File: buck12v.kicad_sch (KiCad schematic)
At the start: 20 parts, among them J5 Conn_01x02, J6 Conn_01x02, Q10 Q_NMOS, Q7 Q_NMOS, Q8 Q_NMOS, U2 LM5148RGYR

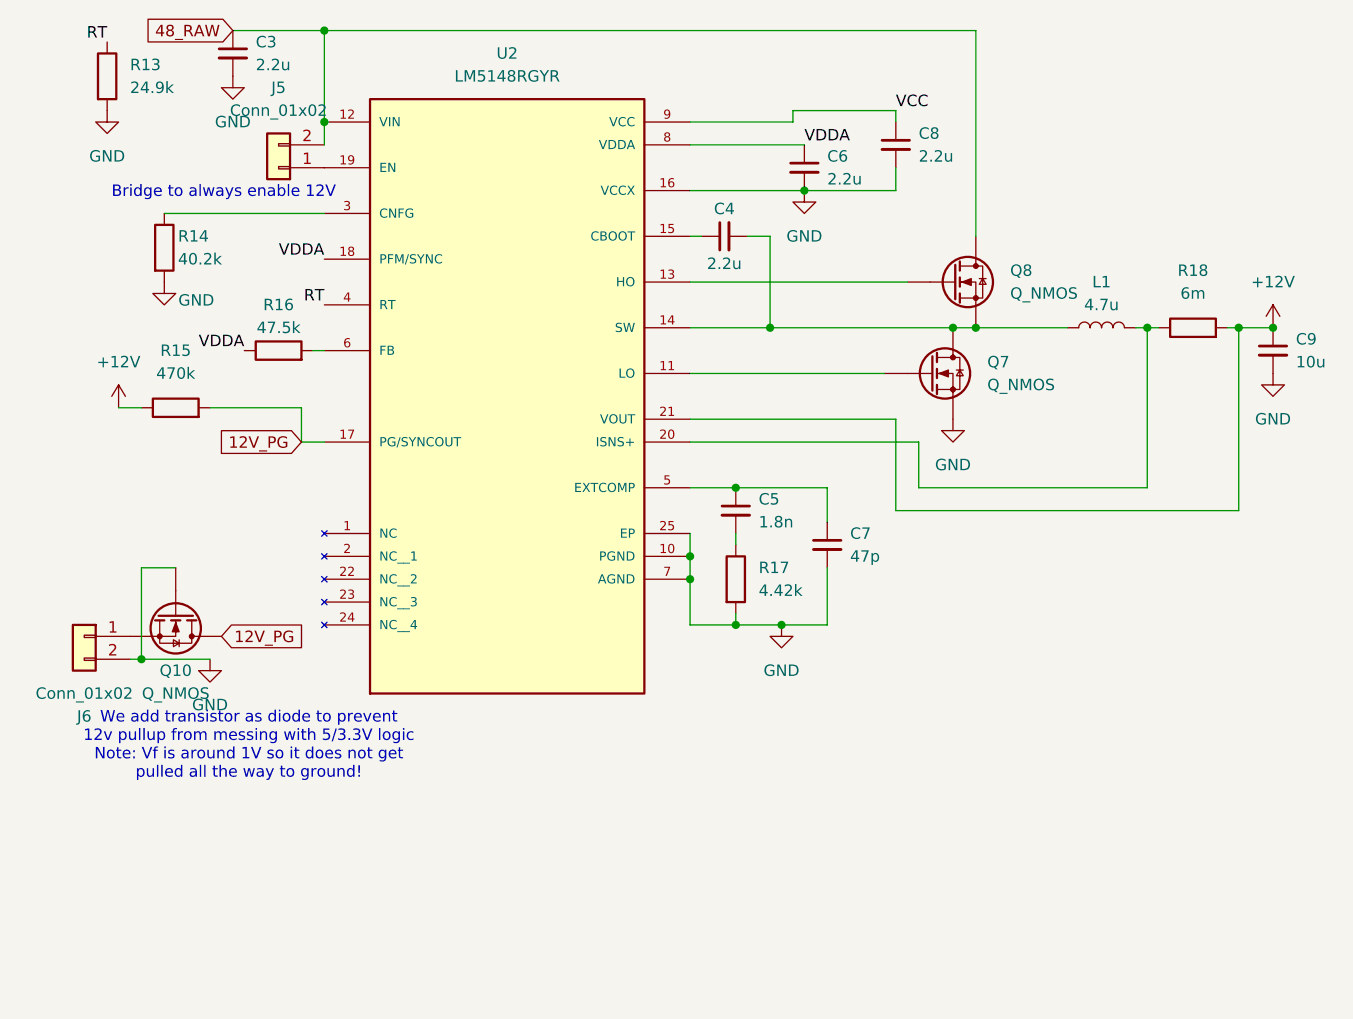
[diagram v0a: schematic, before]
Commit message: added footprints and standardized EN headers
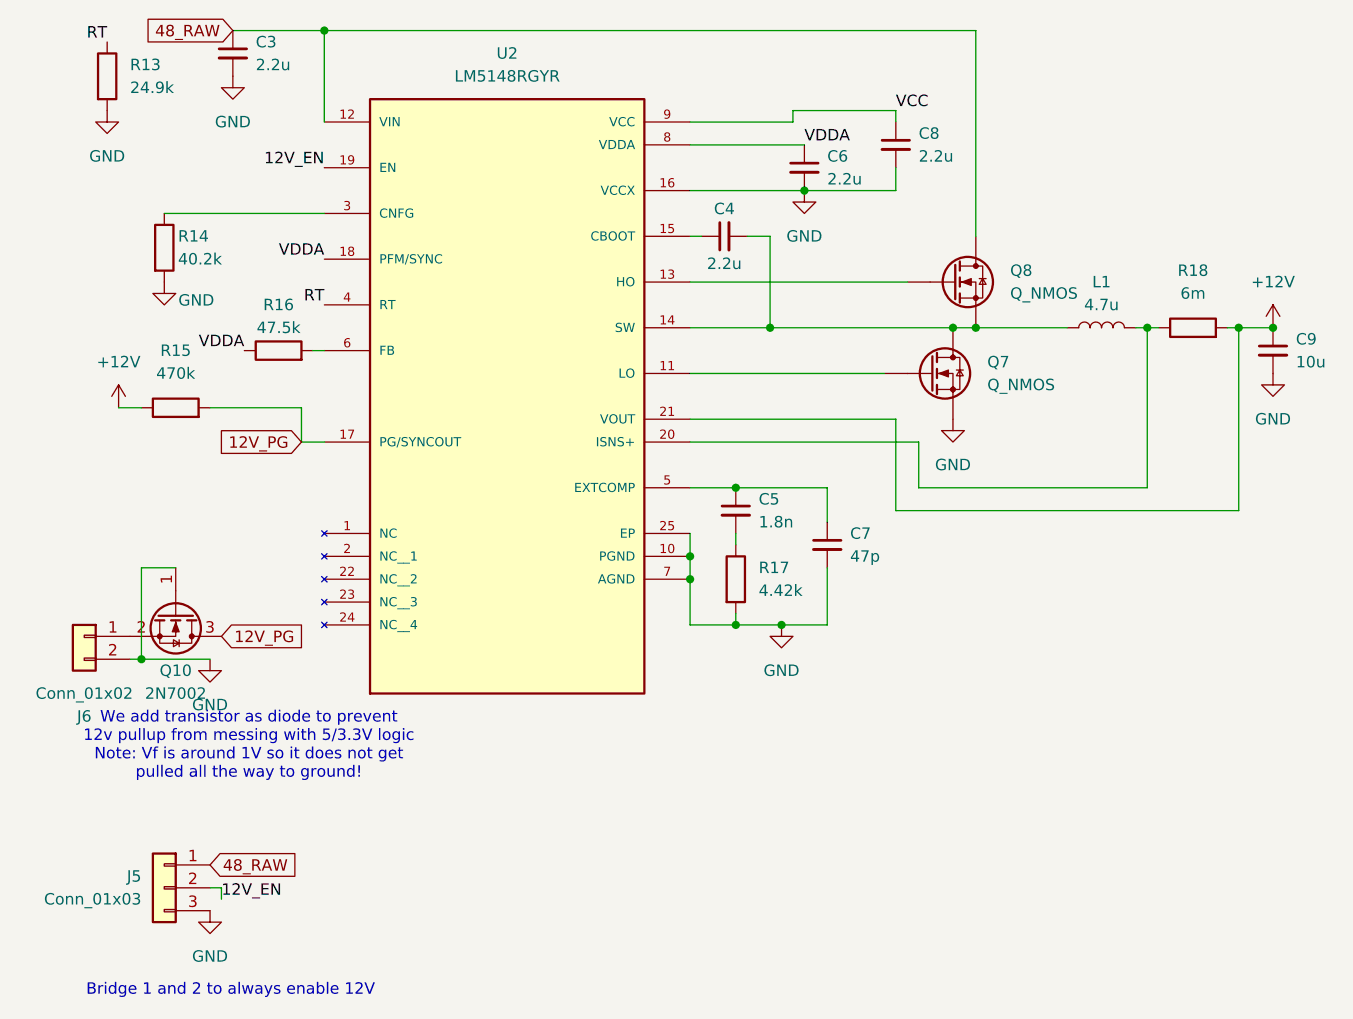
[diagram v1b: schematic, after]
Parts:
- removed J5: Conn_01x02, symbol Connector_Generic:Conn_01x02
- removed Q10: Q_NMOS, symbol Device:Q_NMOS
- added J5: Conn_01x03, Connector_PinHeader_2.54mm:PinHeader_1x03_P2.54mm_Vertical, symbol Connector_Generic:Conn_01x03
- added Q10: 2N7002, Package_TO_SOT_SMD:SOT-23, symbol Transistor_FET:2N7002
- J6: footprint (none) -> Connector_PinHeader_2.54mm:PinHeader_1x02_P2.54mm_Vertical
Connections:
- net 12V_PG: now also Q10.3 (D)
- net 48_RAW: now also J5.1 (Pin_1)
- net GND: now also J5.3 (Pin_3), Q10.1 (G)
- net at J6.1 (Pin_1): now also Q10.2 (S)
- net 12V_EN: now reaches U2.19 (EN)
- net 12V_EN: now also J5.2 (Pin_2)
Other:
- note added: "Bridge 1 and 2 to always enable 12V"
- note removed: "Bridge to always enable 12V"

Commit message: pcb routing
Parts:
- R15: footprint (none) -> Resistor_SMD:R_0201_0603Metric_Pad0.64x0.40mm_HandSolder
- R18: value 6m -> 6m 1W; footprint (none) -> Resistor_SMD:R_1206_3216Metric_Pad1.30x1.75mm_HandSolder
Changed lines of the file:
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@@
 			)
 		)
-		(property "Datasheet" "~"
+		(property "Datasheet" "CODACA"
 			(at 129.54 49.53 0)
 			(effects
@@
 			)
 		)
-		(property "Footprint" ""
+		(property "Footprint" "Resistor_SMD:R_0201_0603Metric_Pad0.64x0.40mm_HandSolder"
 			(at 26.67 60.198 90)
 			(effects
@@
 			)
 		)
-		(property "Value" "6m"
+		(property "Value" "6m 1W"
 			(at 139.7 45.72 90)
 			(effects
@@
 			)
 		)
-		(property "Footprint" ""
+		(property "Footprint" "Resistor_SMD:R_1206_3216Metric_Pad1.30x1.75mm_HandSolder"
 			(at 139.7 51.308 90)
 			(effects

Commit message: final push
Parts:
- L1: value 4.7u -> 3.7; footprint (none) -> footprints:P1173.372NL
- Q7, Q8: footprint (none) -> Package_TO_SOT_SMD:TO-252-2; symbol Device:Q_NMOS -> xt90:NMOS_for_footprint
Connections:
- net 48_RAW: now also Q8.2 (D); no longer Q8.D
- net GND: now also Q7.3 (S); no longer Q7.S
- net at C4.2, L1.1, U2.14 (SW): now also Q7.2 (D), Q8.3 (S); no longer Q7.D, Q8.S
- net at U2.11 (LO): now also Q7.1 (G); no longer Q7.G
- net at U2.13 (HO): now also Q8.1 (G); no longer Q8.G
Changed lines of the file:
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@@
 		)
 		(instances
+			(project "buck12v"
+				(path "/77db3944-8136-4a9d-8d46-d8c78d169ccf"
+					(reference "Q?")
+					(unit 1)
+				)
+			)
 			(project ""
 				(path "/883cb7fa-3eb5-48d4-9cde-7c11307d94f0/ccf07133-5d0c-4081-9a30-ebff06623cf2"
@@
 	)
 	(symbol
-		(lib_id "Device:Q_NMOS")
+		(lib_id "xt90:NMOS_for_footprint")
 		(at 110.49 54.61 0)
 		(unit 1)
@@
 			)
 		)
-		(property "Footprint" ""
+		(property "Footprint" "Package_TO_SOT_SMD:TO-252-2"
 			(at 115.57 52.07 0)
 			(effects
@@
 			)
 		)
-		(pin "S"
-		)
-		(pin "D"
-		)
-		(pin "G"
+		(pin "2"
+		)
+		(pin "3"
+		)
+		(pin "1"
 		)
 		(instances
@@
 		)
 		(instances
+			(project "buck12v"
+				(path "/77db3944-8136-4a9d-8d46-d8c78d169ccf"
+					(reference "J?")
+					(unit 1)
+				)
+			)
 			(project "doggie_board"
 				(path "/883cb7fa-3eb5-48d4-9cde-7c11307d94f0/ccf07133-5d0c-4081-9a30-ebff06623cf2"
@@
 			)
 		)
-		(property "Value" "4.7u"
+		(property "Value" "3.7"
 			(at 129.54 46.99 90)
 			(effects
@@
 			)
 		)
-		(property "Footprint" ""
+		(property "Footprint" "footprints:P1173.372NL"
 			(at 129.54 49.53 0)
 			(effects
@@
 		)
 		(instances
+			(project "buck12v"
+				(path "/77db3944-8136-4a9d-8d46-d8c78d169ccf"
+					(reference "J?")
+					(unit 1)
+				)
+			)
 			(project "doggie_board"
 				(path "/883cb7fa-3eb5-48d4-9cde-7c11307d94f0/ccf07133-5d0c-4081-9a30-ebff06623cf2"
@@
 		)
 		(instances
+			(project "buck12v"
+				(path "/77db3944-8136-4a9d-8d46-d8c78d169ccf"
+					(reference "R?")
+					(unit 1)
+				)
+			)
 			(project ""
 				(path "/883cb7fa-3eb5-48d4-9cde-7c11307d94f0/ccf07133-5d0c-4081-9a30-ebff06623cf2"
@@
 		)
 		(instances
+			(project "buck12v"
+				(path "/77db3944-8136-4a9d-8d46-d8c78d169ccf"
+					(reference "#PWR?")
+					(unit 1)
+				)
+			)
 			(project "doggie_board"
 				(path "/883cb7fa-3eb5-48d4-9cde-7c11307d94f0/ccf07133-5d0c-4081-9a30-ebff06623cf2"
@@
 	)
 	(symbol
-		(lib_id "Device:Q_NMOS")
+		(lib_id "xt90:NMOS_for_footprint")
 		(at 113.03 44.45 0)
 		(unit 1)
@@
 			)
 		)
-		(property "Footprint" ""
+		(property "Footprint" "Package_TO_SOT_SMD:TO-252-2"
 			(at 118.11 41.91 0)
 			(effects
@@
 			)
 		)
-		(pin "S"
-		)
-		(pin "D"
-		)
-		(pin "G"
+		(pin "1"
+		)
+		(pin "2"
+		)
+		(pin "3"
 		)
 		(instances
@@
 		)
 		(instances
+			(project "buck12v"
+				(path "/77db3944-8136-4a9d-8d46-d8c78d169ccf"
+					(reference "#PWR?")
+					(unit 1)
+				)
+			)
 			(project ""
 				(path "/883cb7fa-3eb5-48d4-9cde-7c11307d94f0/ccf07133-5d0c-4081-9a30-ebff06623cf2"
@@
 		)
 		(instances
+			(project "buck12v"
+				(path "/77db3944-8136-4a9d-8d46-d8c78d169ccf"
+					(reference "#PWR?")
+					(unit 1)
+				)
+			)
 			(project ""
 				(path "/883cb7fa-3eb5-48d4-9cde-7c11307d94f0/ccf07133-5d0c-4081-9a30-ebff06623cf2"

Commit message: om suggestions
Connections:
- net switch 12v: now reaches C4.2, L1.1, Q7.2 (D), Q8.3 (S), U2.14 (SW)
- net low_fet: now reaches Q7.1 (G), U2.11 (LO)
- net sense: now reaches L1.2, R18.1, U2.20 (ISNS+)
- net high_fet: now reaches Q8.1 (G), U2.13 (HO)
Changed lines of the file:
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@@
+		)
+	)
+	(label "high_fet"
+		(at 100.33 44.45 0)
+		(effects
+			(font
+				(size 1.27 1.27)
+			)
+			(justify left bottom)
 		)
 	)
@@
 			)
 			(justify right bottom)
+		)
+	)
+	(label "low_fet"
+		(at 95.25 54.61 0)
+		(effects
+			(font
+				(size 1.27 1.27)
+			)
+			(justify left bottom)
 		)
 	)
@@
 		)
 	)
+	(label "sense"
+		(at 134.62 49.53 90)
+		(effects
+			(font
+				(size 1.27 1.27)
+			)
+			(justify left bottom)
+		)
+	)
 	(label "RT"
 		(at 43.18 46.99 180)
@@
 		)
 	)
+	(label "switch 12v"
+		(at 95.25 49.53 0)
+		(effects
+			(font
+				(size 1.27 1.27)
+			)
+			(justify left bottom)
+		)
+	)

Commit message: fixed footprintns
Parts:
- C3, C4, C5, C6, C7, C8, C9: footprint Capacitor_SMD:C_0201_0603Metric_Pad0.64x0.40mm_HandSolder -> Capacitor_SMD:C_0603_1608Metric_Pad1.08x0.95mm_HandSolder
- R13, R14, R15, R16, R17: footprint Resistor_SMD:R_0201_0603Metric_Pad0.64x0.40mm_HandSolder -> Resistor_SMD:R_0603_1608Metric_Pad0.98x0.95mm_HandSolder
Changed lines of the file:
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@@
 			)
 		)
-		(property "Footprint" "Resistor_SMD:R_0201_0603Metric_Pad0.64x0.40mm_HandSolder"
+		(property "Footprint" "Resistor_SMD:R_0603_1608Metric_Pad0.98x0.95mm_HandSolder"
 			(at 23.622 40.64 90)
 			(effects
@@
 			)
 		)
-		(property "Footprint" "Capacitor_SMD:C_0201_0603Metric_Pad0.64x0.40mm_HandSolder"
+		(property "Footprint" "Capacitor_SMD:C_0603_1608Metric_Pad1.08x0.95mm_HandSolder"
 			(at 87.63 39.37 0)
 			(effects
@@
 			)
 		)
-		(property "Footprint" "Capacitor_SMD:C_0201_0603Metric_Pad0.64x0.40mm_HandSolder"
+		(property "Footprint" "Capacitor_SMD:C_0603_1608Metric_Pad1.08x0.95mm_HandSolder"
 			(at 148.59 52.07 0)
 			(effects
@@
 			)
 		)
-		(property "Footprint" "Capacitor_SMD:C_0201_0603Metric_Pad0.64x0.40mm_HandSolder"
+		(property "Footprint" "Capacitor_SMD:C_0603_1608Metric_Pad1.08x0.95mm_HandSolder"
 			(at 33.02 19.05 0)
 			(effects
@@
 			)
 		)
-		(property "Footprint" "Capacitor_SMD:C_0201_0603Metric_Pad0.64x0.40mm_HandSolder"
+		(property "Footprint" "Capacitor_SMD:C_0603_1608Metric_Pad1.08x0.95mm_HandSolder"
 			(at 88.9 69.85 0)
 			(effects
@@
 			)
 		)
-		(property "Footprint" "Resistor_SMD:R_0201_0603Metric_Pad0.64x0.40mm_HandSolder"
+		(property "Footprint" "Resistor_SMD:R_0603_1608Metric_Pad0.98x0.95mm_HandSolder"
 			(at 17.272 21.59 90)
 			(effects
@@
 			)
 		)
-		(property "Footprint" "Capacitor_SMD:C_0201_0603Metric_Pad0.64x0.40mm_HandSolder"
+		(property "Footprint" "Capacitor_SMD:C_0603_1608Metric_Pad1.08x0.95mm_HandSolder"
 			(at 106.68 29.21 0)
 			(effects
@@
 			)
 		)
-		(property "Footprint" "Resistor_SMD:R_0201_0603Metric_Pad0.64x0.40mm_HandSolder"
+		(property "Footprint" "Resistor_SMD:R_0603_1608Metric_Pad0.98x0.95mm_HandSolder"
 			(at 26.67 60.198 90)
 			(effects
@@
 			)
 		)
-		(property "Footprint" "Capacitor_SMD:C_0201_0603Metric_Pad0.64x0.40mm_HandSolder"
+		(property "Footprint" "Capacitor_SMD:C_0603_1608Metric_Pad1.08x0.95mm_HandSolder"
 			(at 96.52 31.75 0)
 			(effects
@@
 			)
 		)
-		(property "Footprint" "Resistor_SMD:R_0201_0603Metric_Pad0.64x0.40mm_HandSolder"
+		(property "Footprint" "Resistor_SMD:R_0603_1608Metric_Pad0.98x0.95mm_HandSolder"
 			(at 38.1 53.848 90)
 			(effects
@@
 			)
 		)
-		(property "Footprint" "Capacitor_SMD:C_0201_0603Metric_Pad0.64x0.40mm_HandSolder"
+		(property "Footprint" "Capacitor_SMD:C_0603_1608Metric_Pad1.08x0.95mm_HandSolder"
 			(at 99.06 73.66 0)
 			(effects
@@
 			)
 		)
-		(property "Footprint" "Resistor_SMD:R_0201_0603Metric_Pad0.64x0.40mm_HandSolder"
+		(property "Footprint" "Resistor_SMD:R_0603_1608Metric_Pad0.98x0.95mm_HandSolder"
 			(at 87.122 77.47 90)
 			(effects

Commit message: updated headers
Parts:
- removed J5: Conn_01x03, Connector_PinHeader_2.54mm:PinHeader_1x03_P2.54mm_Vertical, symbol Connector_Generic:Conn_01x03
- removed J6: Conn_01x02, Connector_PinHeader_2.54mm:PinHeader_1x02_P2.54mm_Vertical, symbol Connector_Generic:Conn_01x02
- removed Q10: 2N7002, Package_TO_SOT_SMD:SOT-23, symbol Transistor_FET:2N7002
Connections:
- net +12V: no longer R15.1
- new net +3.3V_LP: R15.1
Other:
- note removed: "Bridge 1 and 2 to always enable 12V"
- note removed: "We add transistor as diode to prevent 12v pullup from messing with 5/3.3V logic Note: Vf is around 1V so it does not get pulled all the way to ground!"
- moved on the sheet: R15

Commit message: upadated board to use 2 power layers
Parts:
- U2: footprint footprints:QFN50P550X350X100-25N -> footprints:LM5148RGYR
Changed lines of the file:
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@@
 			)
 		)
-		(property "Footprint" "footprints:QFN50P550X350X100-25N"
+		(property "Footprint" "footprints:LM5148RGYR"
 			(at 63.5 52.07 0)
 			(effects
